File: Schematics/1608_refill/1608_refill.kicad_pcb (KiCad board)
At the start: 2 copper layers, 100 x 100 mm, 80 parts, among them J1 USB_B_Micro, J10 Switch 2, J11 Switch 3, J12 Switch 1, J13 SWD, J14 SWD, J15 Screen data, J16 Screen Backlight, J2 Pot 1, J3 Barrel_Jack_Switch, J4 USB_BOOT, J5 Load Cell Power, J6 Load Cell Data, J7 Inductor 1, J8 Inductor 2, J9 Pot 2, Q1 TIP120, Q2 TIP120, SW4 SW_SPDT, U1 RP2040, U2 NCP1117-3.3_SOT223, U3 Flash Memory, U5 AD622, Y1 Crystal

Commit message: gearing up for PCB 2
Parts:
- added R17: 200, Resistor_SMD:R_0603_1608Metric_Pad0.98x0.95mm_HandSolder, F.Cu at (143.5, 87.4)
- added R18: 200, Resistor_SMD:R_0603_1608Metric_Pad0.98x0.95mm_HandSolder, F.Cu at (143.6, 95.2)
- moved C1 29.2 mm to (114.3, 123.7), turned to 0 degrees
- moved C16 27.4 mm to (92.6, 126.4), turned to 0 degrees
- moved R12 26.2 mm to (126.2, 156.8)
- moved R15 26.1 mm to (129.7, 113.7), turned to 0 degrees
- moved Y1 22.6 mm to (101.2, 150.0)
- moved C5 21.9 mm to (92.6, 157.0)
- moved C6 21.9 mm to (106.7, 157.0)
- moved D7 20.9 mm to (119.3, 145.0)
- moved J6 20.9 mm to (140.4, 140.4)
- moved D6 20.9 mm to (119.3, 134.3)
- moved U5 20.9 mm to (118.8, 144.3)
- moved C11 20.7 mm to (110.0, 136.8)
- moved R11 20.4 mm to (100.3, 141.7)
- moved C8 20.4 mm to (123.1, 116.5), turned to 180 degrees
- moved ADC 20.0 mm to (130.0, 125.6)
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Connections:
- J2 pad 2: /P1 -> Net-(J2-Pad2)
- J9 pad 2: /P2 -> Net-(J9-Pad2)
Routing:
- net +12V: track 98.4 -> 0.57 mm
- net /SWCLK: track 65.9 -> 0.90 mm
- net /SWD: track 64.3 -> 2.60 mm
- net /SW3: track 53.8 -> 0.00 mm
- net /P2: track 52.2 -> 0.00 mm, vias 2 -> 1
- net GND: track 58.5 -> 6.87 mm, vias 21 -> 5
- net /SW2: track 47.6 -> 0.00 mm
- net /P1: track 47.1 -> 0.00 mm, vias 2 -> 0
- net Net-(J9-Pad2): track 0.00 -> 44.4 mm
- net /SW1: track 44.0 -> 0.00 mm
- net Net-(J2-Pad2): track 0.00 -> 38.5 mm, vias 0 -> 1
- net /QSPI_SS: track 37.5 -> 2.51 mm
- net /QSPI_SD1: track 27.6 -> 0.00 mm
- net /ADC0: track 36.4 -> 10.3 mm
- net /V2: track 19.9 -> 0.00 mm
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
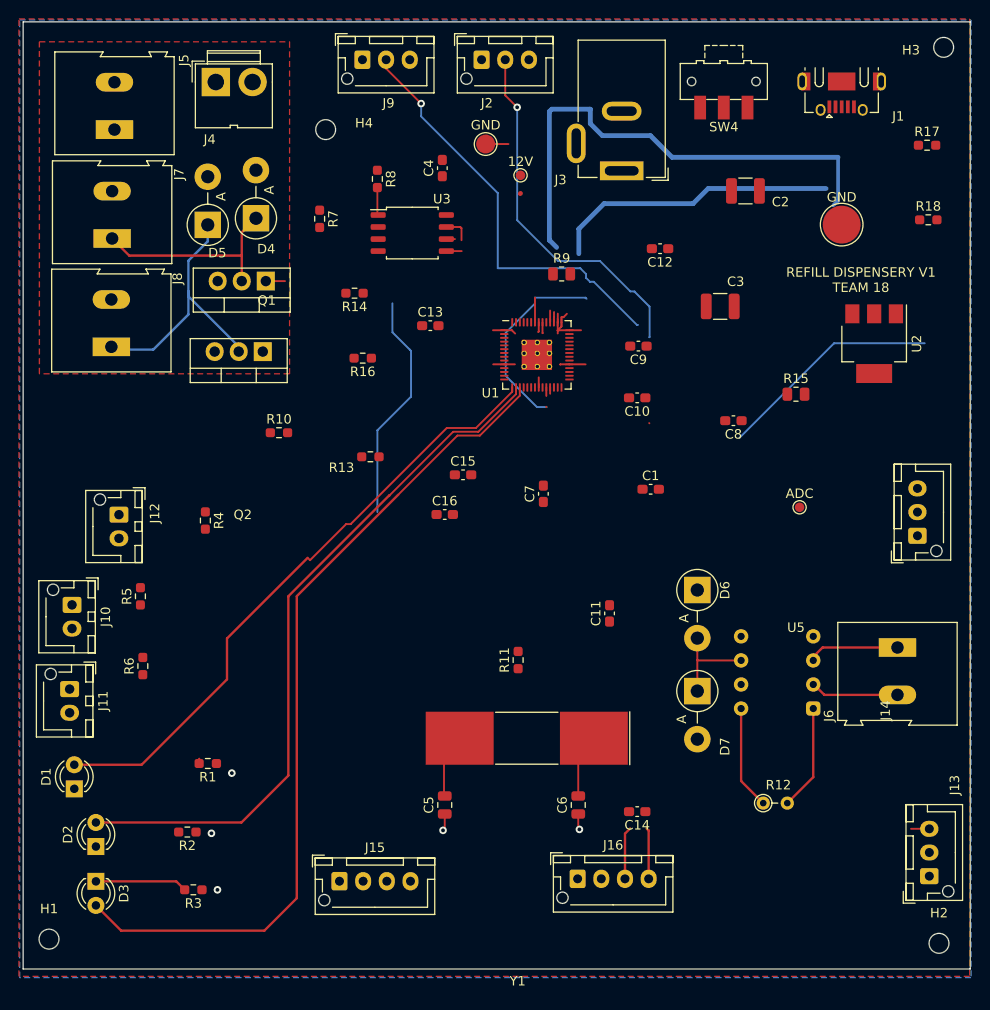
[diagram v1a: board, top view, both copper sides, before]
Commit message: 1608:all routes connected
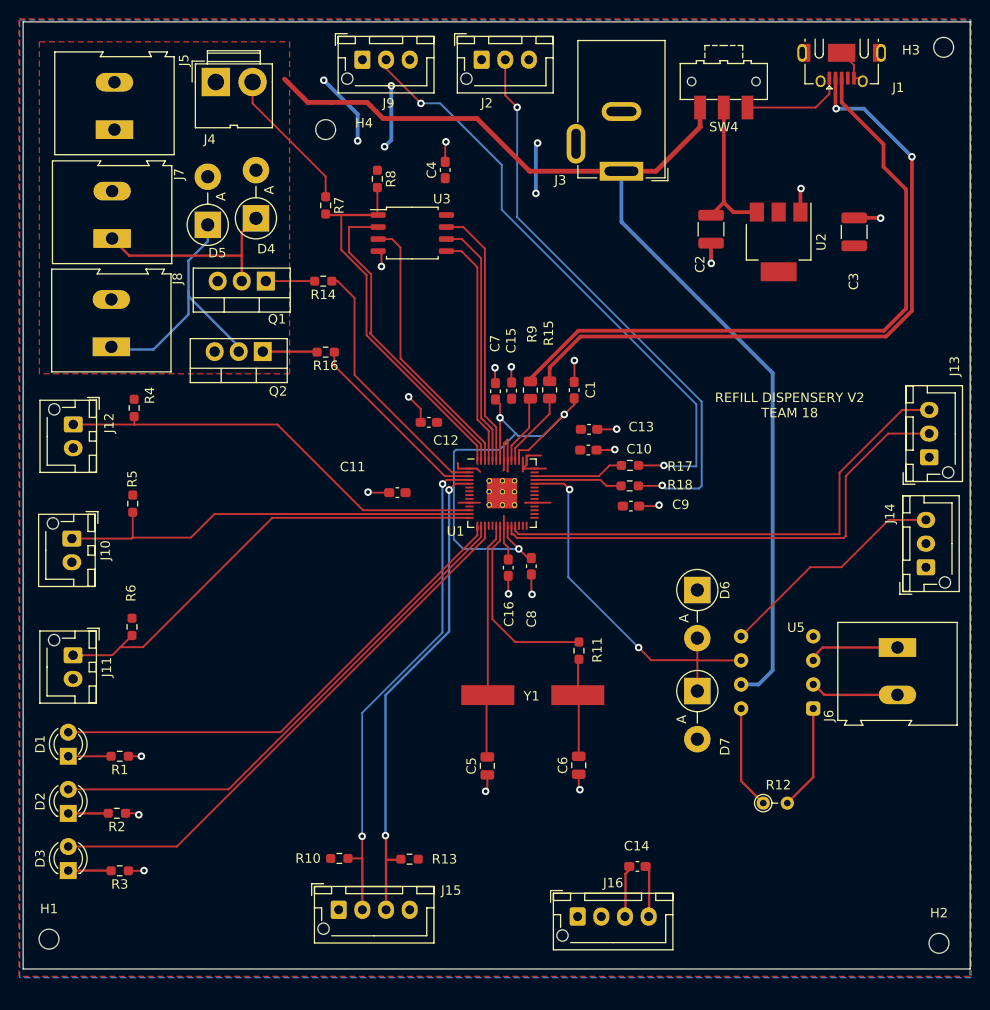
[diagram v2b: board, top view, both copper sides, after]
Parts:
- removed 12V, ADC: TestPoint_Pad_D1.0mm, TestPoint:TestPoint_Pad_D1.0mm
- removed GND: TestPoint_Pad_D4.0mm, TestPoint:TestPoint_Pad_D4.0mm
- removed GND: TestPoint_Pad_D2.0mm, TestPoint:TestPoint_Pad_D2.0mm
- Y1: footprint Crystal:Crystal_SMD_SeikoEpson_MA505-2Pin_12.7x5.1mm_HandSoldering -> Library:ABLS12MHZ
- moved R17 46.1 mm to (112.1, 121.2), turned to 180 degrees
- moved R10 45.4 mm to (81.5, 162.7)
- moved J13 44.2 mm to (143.7, 120.3)
- moved R13 42.7 mm to (88.9, 162.8)
- moved R18 42.2 mm to (112.1, 123.3), turned to 180 degrees
- moved C12 30.5 mm to (90.9, 116.6)
- moved C8 26.3 mm to (101.7, 131.8), turned to -90 degrees
- moved R15 26.0 mm to (103.7, 113.2), turned to -90 degrees
- moved C11 25.8 mm to (87.6, 124.1), turned to 180 degrees
- moved C13 20.0 mm to (107.8, 117.4)
- moved C9 16.9 mm to (112.2, 125.5), turned to 0 degrees
- moved C3 16.2 mm to (135.8, 96.5), turned to 90 degrees
- moved ? 15.1 mm to (97.3, 124.0)
- moved ? 15.1 mm to (99.9, 125.3)
- moved ? 15.1 mm to (97.3, 122.8)
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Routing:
- net +12V: track 0.57 -> 115.2 mm
- net /SWCLK: track 0.90 -> 53.9 mm
- net /S_SDA: track 0.00 -> 53.0 mm, vias 0 -> 2
- net /S_SCL: track 0.00 -> 51.1 mm, vias 0 -> 2
- net /SWD: track 2.60 -> 53.6 mm
- net /SW3: track 0.00 -> 49.6 mm
- net /SW1: track 0.00 -> 46.4 mm
- net /SW2: track 0.00 -> 45.8 mm
- net /USB_D-: track 30.5 -> 71.8 mm, vias 0 -> 2
- net GND: track 6.87 -> 45.1 mm, vias 5 -> 20
- net /QSPI_SS: track 2.51 -> 40.0 mm
- net /QSPI_SD1: track 0.00 -> 33.7 mm
- net /ADC0: track 10.3 -> 40.8 mm, vias 0 -> 2
- net /LED3: track 88.8 -> 58.8 mm
- net +1V1: track 24.4 -> 53.7 mm, vias 0 -> 3
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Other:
- board text added: "REFILL DISPENSERY V2 TEAM 18"
- board text removed: "REFILL DISPENSERY V1 TEAM 18"

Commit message: 1608 mostly done
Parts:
- R12: footprint Resistor_THT:R_Axial_DIN0204_L3.6mm_D1.6mm_P2.54mm_Vertical -> Resistor_THT:R_Axial_DIN0204_L3.6mm_D1.6mm_P7.62mm_Horizontal
- moved R12 3.83 mm to (123.9, 153.8)
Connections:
- R16 pad 1: /V2 -> Net-(Q2-Pad1)
- R16 pad 2: Net-(Q2-Pad1) -> /V2
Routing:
- net /V2: track 20.5 -> 26.3 mm
- net Net-(Q2-Pad1): track 5.75 -> 0.00 mm
- net +3.3V: track 46.4 -> 51.2 mm
- net Net-(R12-Pad2): track 11.1 -> 6.98 mm
- net Net-(R12-Pad1): track 11.0 -> 6.98 mm
